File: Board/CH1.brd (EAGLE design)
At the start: 162.5 x 69.5 mm, 34 parts, among them IC3 MCP2300X/SO, IC6 74LS595D, Q1 3.6864MHz, U1 328P

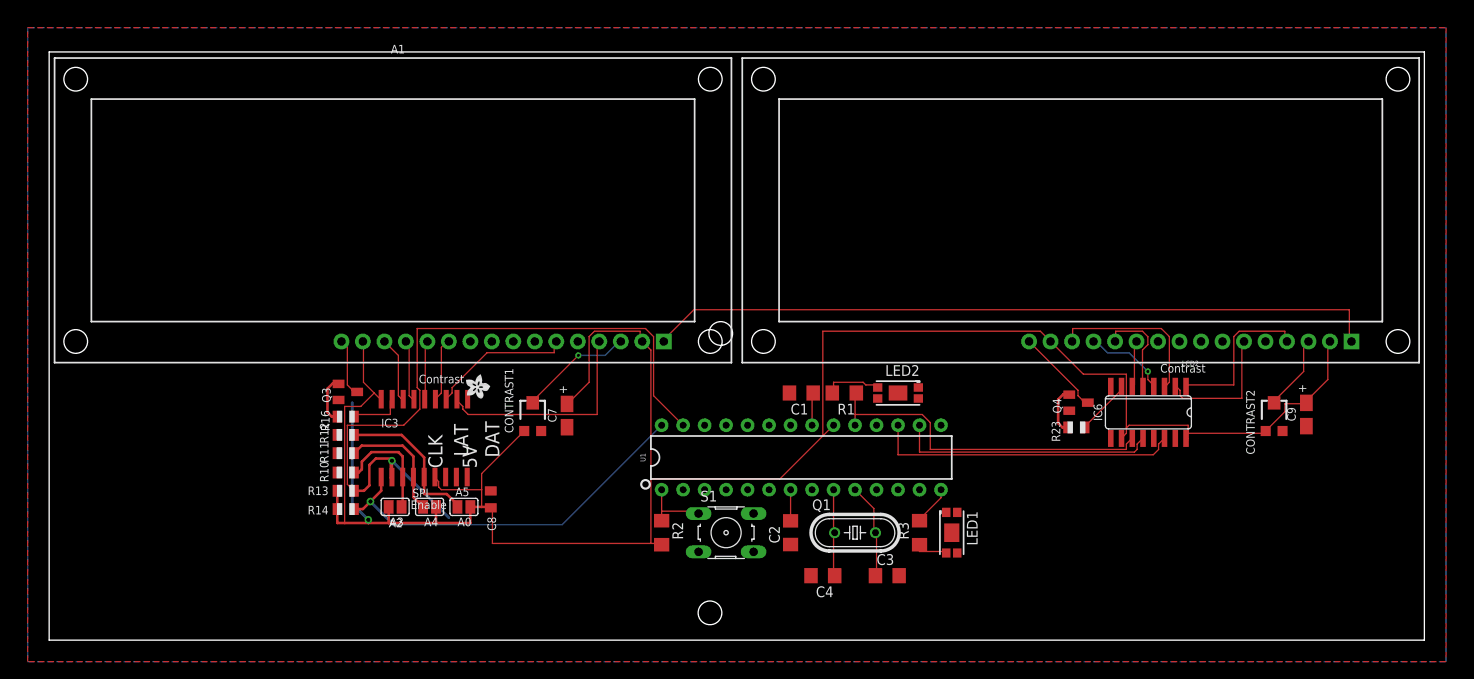
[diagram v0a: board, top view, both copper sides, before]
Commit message: Changes to board, checked autorouter, via and trace size. ToDo: Check silk.
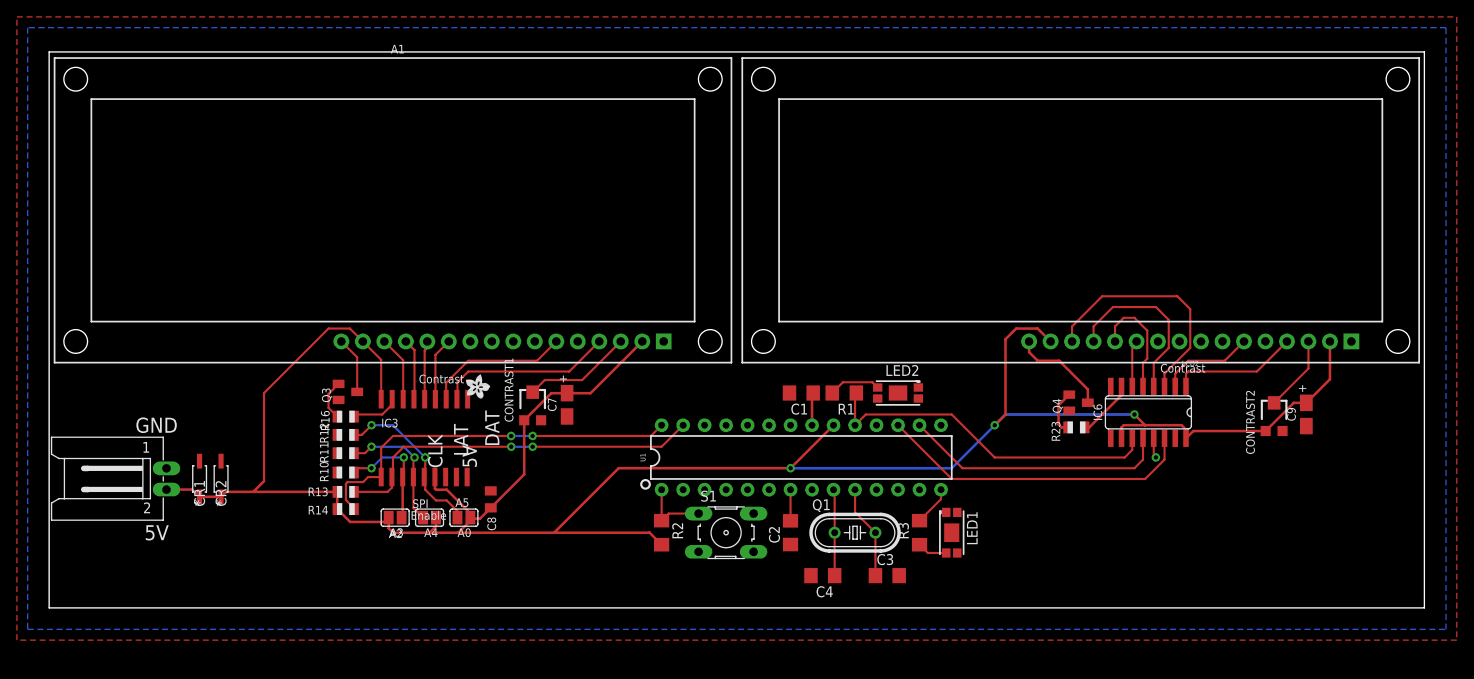
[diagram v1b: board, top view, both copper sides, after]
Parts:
- added CR1: BZT52C5V1-7-F, trigger_pcb_library:SOD123
- added CR2: BAV16W-7-F, trigger_pcb_library:SOD123
- added SV1: (no value), con-amp-mt:L02P
- moved A3 1.27 mm to (40.9, 45.0)
- moved A4 1.27 mm to (45.0, 45.0)
- moved A5 1.27 mm to (49.0, 45.0)
- moved C7 1.27 mm to (61.2, 58.3)
- moved CONTRAST1 1.27 mm to (57.1, 58.3)
- moved R13 0.13 mm to (35.1, 48.0)
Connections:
- removed net VSS: LCD1.1, LCD2.1
- net GND: now also CR1.2, CR2.2, LCD1.1, LCD2.1, SV1.1
- net VCC: now also CR1.1, CR2.1, SV1.2
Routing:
- net VSS: track 86.5 -> 0.00 mm
- net SDA: track 88.6 -> 44.1 mm, vias 1 -> 2
- net SPI_DB6: track 9.91 -> 20.8 mm, vias 1 -> 0
- net VCC: track 269.4 -> 279.1 mm, vias 1 -> 3
- net SPI_DB7: track 19.5 -> 28.2 mm
- net I2C_RS: track 26.4 -> 20.8 mm
- net SPI_E: track 15.7 -> 11.2 mm
- net SPI_RS: track 19.0 -> 15.0 mm
- net GND: track 0.02 -> 2.37 mm, vias 0 -> 1
- net SPI_DB5: track 11.4 -> 13.4 mm
- net N$14: track 18.5 -> 20.0 mm, vias 0 -> 2
- net MOSI: track 36.2 -> 37.6 mm
- net N$15: track 14.4 -> 15.6 mm, vias 0 -> 2
- net N$19: track 5.78 -> 4.79 mm
- net N$18: track 7.59 -> 6.74 mm
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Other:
- board size 162.5 x 69.5 mm -> 162.5 x 65.7 mm
- board text added: "GND"
